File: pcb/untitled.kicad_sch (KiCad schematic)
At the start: 27 parts, among them IC1 DRV8302DCA

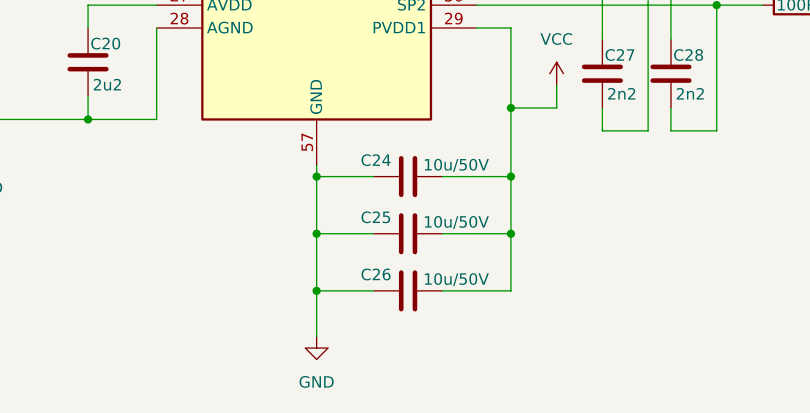
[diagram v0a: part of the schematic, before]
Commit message: pcb: complete bom and first layout
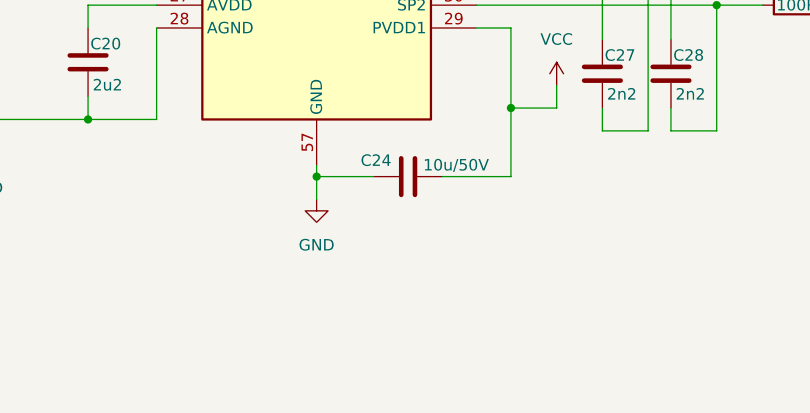
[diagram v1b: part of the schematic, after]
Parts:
- removed C25, C26: 10u/50V, Capacitor_SMD:C_1206_3216Metric, symbol Device:C
- C20: footprint (none) -> Capacitor_SMD:C_0603_1608Metric
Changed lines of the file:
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@@
 	)
 	(junction
-		(at 144.78 144.78)
-		(diameter 0)
-		(color 0 0 0 0)
-	)
-	(junction
 		(at 144.78 132.08)
 		(diameter 0)
@@
 	)
 	(junction
-		(at 166.37 138.43)
-		(diameter 0)
-		(color 0 0 0 0)
-	)
-	(junction
 		(at 219.71 96.52)
 		(diameter 0)
@@
 	)
 	(junction
-		(at 144.78 138.43)
-		(diameter 0)
-		(color 0 0 0 0)
-	)
-	(junction
-		(at 166.37 132.08)
-		(diameter 0)
-		(color 0 0 0 0)
-	)
-	(junction
 		(at 107.95 81.28)
 		(diameter 0)
@@
 	(wire
 		(pts
-			(xy 144.78 138.43) (xy 151.13 138.43)
-		)
-		(stroke
-			(width 0)
-			(type default)
-		)
-	)
-	(wire
-		(pts
 			(xy 162.56 113.03) (xy 189.23 113.03)
 		)
@@
 	(wire
 		(pts
-			(xy 123.19 110.49) (xy 127 110.49)
+			(xy 144.78 132.08) (xy 144.78 134.62)
 		)
 		(stroke
@@
 	(wire
 		(pts
-			(xy 144.78 132.08) (xy 144.78 138.43)
+			(xy 123.19 110.49) (xy 127 110.49)
 		)
 		(stroke
@@
 	(wire
 		(pts
-			(xy 158.75 138.43) (xy 166.37 138.43)
-		)
-		(stroke
-			(width 0)
-			(type default)
-		)
-	)
-	(wire
-		(pts
 			(xy 179.07 67.31) (xy 182.88 67.31)
 		)
@@
 	(wire
 		(pts
-			(xy 166.37 132.08) (xy 166.37 138.43)
-		)
-		(stroke
-			(width 0)
-			(type default)
-		)
-	)
-	(wire
-		(pts
 			(xy 219.71 96.52) (xy 223.52 96.52)
 		)
@@
 	(wire
 		(pts
-			(xy 144.78 130.81) (xy 144.78 132.08)
-		)
-		(stroke
-			(width 0)
-			(type default)
-		)
-	)
-	(wire
-		(pts
 			(xy 162.56 82.55) (xy 165.1 82.55)
 		)
@@
 	(wire
 		(pts
-			(xy 158.75 144.78) (xy 166.37 144.78)
-		)
-		(stroke
-			(width 0)
-			(type default)
-		)
-	)
-	(wire
-		(pts
 			(xy 88.9 93.98) (xy 95.25 93.98)
 		)
@@
 	(wire
 		(pts
-			(xy 144.78 138.43) (xy 144.78 144.78)
-		)
-		(stroke
-			(width 0)
-			(type default)
-		)
-	)
-	(wire
-		(pts
 			(xy 231.14 71.12) (xy 234.95 71.12)
 		)
@@
 	(wire
 		(pts
-			(xy 144.78 144.78) (xy 144.78 149.86)
-		)
-		(stroke
-			(width 0)
-			(type default)
-		)
-	)
-	(wire
-		(pts
-			(xy 166.37 138.43) (xy 166.37 144.78)
+			(xy 144.78 130.81) (xy 144.78 132.08)
 		)
 		(stroke
@@
 	(wire
 		(pts
-			(xy 144.78 144.78) (xy 151.13 144.78)
-		)
-		(stroke
-			(width 0)
-			(type default)
-		)
-	)
-	(wire
-		(pts
 			(xy 189.23 113.03) (xy 194.31 113.03)
 		)
@@
 	(symbol
 		(lib_id "power:GND")
-		(at 144.78 149.86 0)
+		(at 144.78 134.62 0)
 		(unit 1)
 		(exclude_from_sim no)
@@
 		(fields_autoplaced yes)
 		(property "Reference" "#PWR031"
-			(at 144.78 156.21 0)
+			(at 144.78 140.97 0)
 			(effects
 				(font
@@
 		)
 		(property "Value" "GND"
-			(at 144.78 154.94 0)
+			(at 144.78 139.7 0)
 			(effects
 				(font
@@
 		)
 		(property "Footprint" ""
-			(at 144.78 149.86 0)
+			(at 144.78 134.62 0)
 			(effects
 				(font
@@
 		)
 		(property "Datasheet" ""
-			(at 144.78 149.86 0)
+			(at 144.78 134.62 0)
 			(effects
 				(font
@@
 		)
 		(property "Description" "Power symbol creates a global label with name \"GND\" , ground"
-			(at 144.78 149.86 0)
+			(at 144.78 134.62 0)
 			(effects
 				(font
@@
 	)
 	(symbol
-		(lib_id "Device:C")
-		(at 154.94 144.78 90)
-		(unit 1)
-		(exclude_from_sim no)
-		(in_bom yes)
-		(on_board yes)
-		(dnp no)
-		(property "Reference" "C26"
-			(at 151.384 143.002 90)
-			(effects
-				(font
-					(size 1.27 1.27)
-				)
-			)
-		)
-		(property "Value" "10u/50V"
-			(at 160.274 143.51 90)
-			(effects
-				(font
-					(size 1.27 1.27)
-				)
-			)
-		)
-		(property "Footprint" "Capacitor_SMD:C_1206_3216Metric"
-			(at 158.75 143.8148 0)
-			(effects
-				(font
-					(size 1.27 1.27)
-				)
-				(hide yes)
-			)
-		)
-		(property "Datasheet" "~"
-			(at 154.94 144.78 0)
-			(effects
-				(font
-					(size 1.27 1.27)
-				)
-				(hide yes)
-			)
-		)
-		(property "Description" "Unpolarized capacitor"
-			(at 154.94 144.78 0)
-			(effects
-				(font
-					(size 1.27 1.27)
-				)
-				(hide yes)
-			)
-		)
-		(pin "1"
-		)
-		(pin "2"
-		)
-		(instances
-			(project "TractionHub"
-				(path "/c6712b71-1d4c-4b1c-822a-6fd97117379c/719415c5-d6e9-448b-8019-6ea161a5efc2"
-					(reference "C26")
-					(unit 1)
-				)
-			)
-		)
-	)
-	(symbol
 		(lib_id "Device:R")
 		(at 227.33 71.12 90)
@@
 			)
 		)
-		(property "Footprint" ""
+		(property "Footprint" "Capacitor_SMD:C_0603_1608Metric"
 			(at 120.3452 123.19 0)
 			(effects
@@
 					(unit 1)
 				)
-			)
-		)
-	)
-	(symbol
-		(lib_id "Device:C")
-		(at 154.94 138.43 90)
-		(unit 1)
-		(exclude_from_sim no)
-		(in_bom yes)
-		(on_board yes)
-		(dnp no)
-		(property "Reference" "C25"
-			(at 151.384 136.652 90)
-			(effects
-				(font
-					(size 1.27 1.27)
-				)
-			)
-		)
-		(property "Value" "10u/50V"
-			(at 160.274 137.16 90)
-			(effects
-				(font
-					(size 1.27 1.27)
-				)
-			)
-		)
-		(property "Footprint" "Capacitor_SMD:C_1206_3216Metric"
-			(at 158.75 137.4648 0)
-			(effects
-				(font
-					(size 1.27 1.27)
-				)
-				(hide yes)
-			)
-		)
-		(property "Datasheet" "~"
-			(at 154.94 138.43 0)
-			(effects
-				(font
-					(size 1.27 1.27)
-				)
-				(hide yes)
-			)
-		)
-		(property "Description" "Unpolarized capacitor"
-			(at 154.94 138.43 0)
-			(effects
-				(font
-					(size 1.27 1.27)
-				)
-				(hide yes)
-			)
-		)
-		(pin "1"
-		)
-		(pin "2"
-		)
-		(instances
-			(project "TractionHub"
-				(path "/c6712b71-1d4c-4b1c-822a-6fd97117379c/719415c5-d6e9-448b-8019-6ea161a5efc2"
-					(reference "C25")
-					(unit 1)
-				)
